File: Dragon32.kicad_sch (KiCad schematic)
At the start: 7 parts, among them IC14 74LS86, IC22 74LS00, IC23 74LS74, IC25 LM393, IC28 74LS393, IC31 74LS02

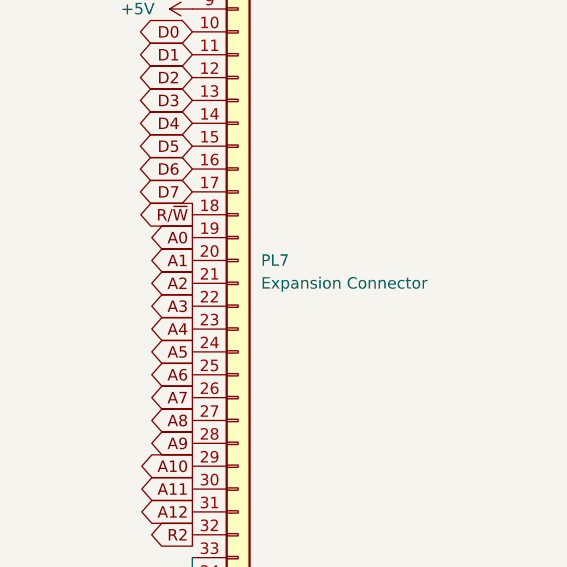
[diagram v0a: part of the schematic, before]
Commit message: revise edge connector
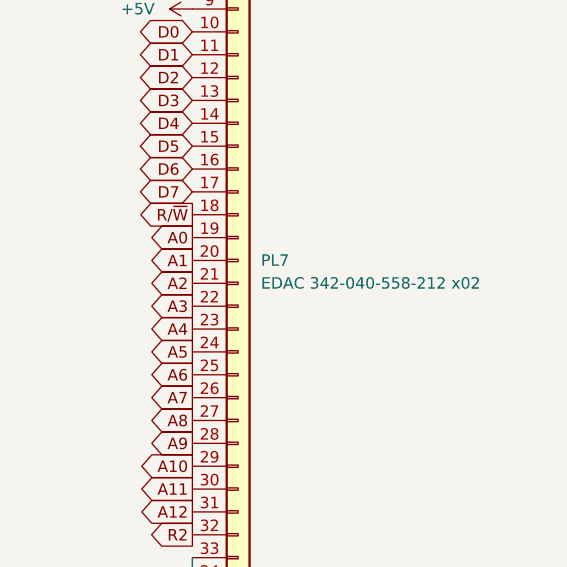
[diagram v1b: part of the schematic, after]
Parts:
- PL7: value Expansion Connector -> EDAC 342-040-558-212 x02; EDAC (none) -> 342-040-558-212
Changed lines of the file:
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@@
       (effects (font (size 1.27 1.27)) hide)
     )
+    (pin "1")
+    (pin "2")
+    (pin "3")
+    (pin "5")
+    (pin "6")
+    (pin "7")
     (pin "4")
     (pin "8")
@@
       (effects (font (size 1.27 1.27)) hide)
     )
+    (pin "1")
+    (pin "2")
+    (pin "3")
+    (pin "4")
+    (pin "5")
+    (pin "6")
+    (pin "10")
+    (pin "11")
+    (pin "12")
+    (pin "13")
+    (pin "8")
+    (pin "9")
     (pin "14")
     (pin "7")
@@
       (effects (font (size 1.27 1.27)) hide)
     )
+    (pin "1")
+    (pin "2")
+    (pin "3")
+    (pin "4")
+    (pin "5")
+    (pin "6")
+    (pin "10")
+    (pin "8")
+    (pin "9")
+    (pin "11")
+    (pin "12")
+    (pin "13")
     (pin "14")
     (pin "7")
@@
       (effects (font (size 1.27 1.27)) hide)
     )
+    (pin "1")
+    (pin "2")
+    (pin "3")
+    (pin "4")
+    (pin "5")
+    (pin "6")
+    (pin "10")
+    (pin "11")
+    (pin "12")
+    (pin "13")
+    (pin "8")
+    (pin "9")
     (pin "14")
     (pin "7")
@@
       (effects (font (size 1.27 1.27)) hide)
     )
+    (pin "1")
+    (pin "2")
+    (pin "3")
+    (pin "4")
+    (pin "5")
+    (pin "6")
+    (pin "10")
+    (pin "8")
+    (pin "9")
+    (pin "11")
+    (pin "12")
+    (pin "13")
     (pin "14")
     (pin "7")
@@
       (effects (font (size 1.27 1.27)) (justify left))
     )
-    (property "Value" "Expansion Connector" (id 1) (at 379.349 88.5189 0)
+    (property "Value" "EDAC 342-040-558-212 x02" (id 1) (at 379.349 88.5189 0)
       (effects (font (size 1.27 1.27)) (justify left))
     )
@@
       (effects (font (size 1.27 1.27)) hide)
     )
-    (property "Datasheet" "~" (id 3) (at 376.809 85.979 0)
+    (property "Datasheet" "https://files.edac.net/edac/content/342/342-040-558-212%20-%20EDAC%20Card%20Edge%20Connector.PDF" (id 3) (at 376.809 85.979 0)
+      (effects (font (size 1.27 1.27)) hide)
+    )
+    (property "EDAC" "342-040-558-212" (id 4) (at 376.809 85.979 0)
       (effects (font (size 1.27 1.27)) hide)
     )
@@
       (effects (font (size 1.27 1.27)) hide)
     )
+    (pin "1")
+    (pin "2")
+    (pin "3")
+    (pin "4")
+    (pin "5")
+    (pin "6")
+    (pin "10")
+    (pin "8")
+    (pin "9")
+    (pin "11")
+    (pin "12")
+    (pin "13")
     (pin "14")
     (pin "7")
@@
     )
     (path "/cc0da426-fd7d-4d0f-a9ed-1df25f1a0b1a"
-      (reference "PL7") (unit 1) (value "Expansion Connector") (footprint "Dragon:Edge_2x20_P2.54mm_Horizontal")
+      (reference "PL7") (unit 1) (value "EDAC 342-040-558-212 x02") (footprint "Dragon:Edge_2x20_P2.54mm_Horizontal")
     )
     (path "/64d8d7b7-14ab-4042-9ee8-f1aec24a139c/9c1d484a-ffa8-4b83-ab66-23bb097dbcf0"

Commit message: cross-reference items to suppliers
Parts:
- IC14: value 74LS86 -> 74LS86N
- IC22: value 74LS00 -> 74LS00N
- IC23: value 74LS74 -> 74ALS74N
- IC25: value LM393 -> LM393P
- IC28: value 74LS393 -> 74LS393N
- IC31: value 74LS02 -> 74LS02N; DigiKey (none) -> 296-1627-5-ND

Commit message: update part numbers
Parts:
- IC14: value 74LS86N -> 74LS86AN; DigiKey (none) -> 296-1669-5-ND
- IC22: DigiKey (none) -> 296-1626-ND
- IC23: DigiKey (none) -> 296-1506-5-ND; Note (none) -> LS74 no longer produced, ALS or HCT instead
- IC25: DigiKey (none) -> 296-1398-5-ND
- IC28: DigiKey (none) -> 296-1665-5-ND
